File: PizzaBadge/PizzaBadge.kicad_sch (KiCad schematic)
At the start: 169 parts, among them J1 BATTERY, J2 signal 1, J3 signal 1, J4 signal 1, J5 signal 1, J6 signal 1, J7 signal 1, J8 signal 1, J9 signal 1, Q1 NPN, Q2 NPN, Q3 NPN, Q4 NPN, Q5 NPN, Q6 NPN, Q7 NPN, Q8 NPN

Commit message: fix scheme, fix board, add reset button, revision1
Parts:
- added J10: signal 1, Connector_PinHeader_2.54mm:PinHeader_1x01_P2.54mm_Vertical, symbol Connector:Conn_01x01_Female
- added R81: 1K, Resistor_THT:R_Axial_DIN0204_L3.6mm_D1.6mm_P7.62mm_Horizontal, symbol Device:R
- added SW1: RESET, Button_Switch_SMD:SW_SPST_CK_RS282G05A3, symbol Switch:SW_Push
- R10, R20, R30, R39, R50, R60, R70, R80: value 4k7 -> 1K
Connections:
- net GND: now also D19.1 (K), D20.1 (K), D21.1 (K), D22.1 (K), D23.1 (K), D24.1 (K), D25.1 (K), D26.1 (K), D27.1 (K), D28.1 (K), D29.1 (K), D30.1 (K), D31.1 (K), D32.1 (K), D33.1 (K), D34.1 (K), D35.1 (K), D36.1 (K), D37.1 (K), D38.1 (K), D39.1 (K), D40.1 (K), D41.1 (K), D42.1 (K), D43.1 (K), D44.1 (K), D45.1 (K), D46.1 (K), D47.1 (K), D48.1 (K), D49.1 (K), D50.1 (K), D51.1 (K), D52.1 (K), D53.1 (K), D54.1 (K), D55.1 (K), D56.1 (K), D57.1 (K), D58.1 (K), D59.1 (K), D60.1 (K), D61.1 (K), D62.1 (K), D63.1 (K), D64.1 (K), D65.1 (K), D66.1 (K), D67.1 (K), D68.1 (K), D69.1 (K), D70.1 (K), D71.1 (K), D72.1 (K), SW1.1
- net 12V renamed 5V
- net 5V: now also R81.2
- new net RESET: J10.1 (Pin_1), R81.1, SW1.2
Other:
- moved on the sheet: J1

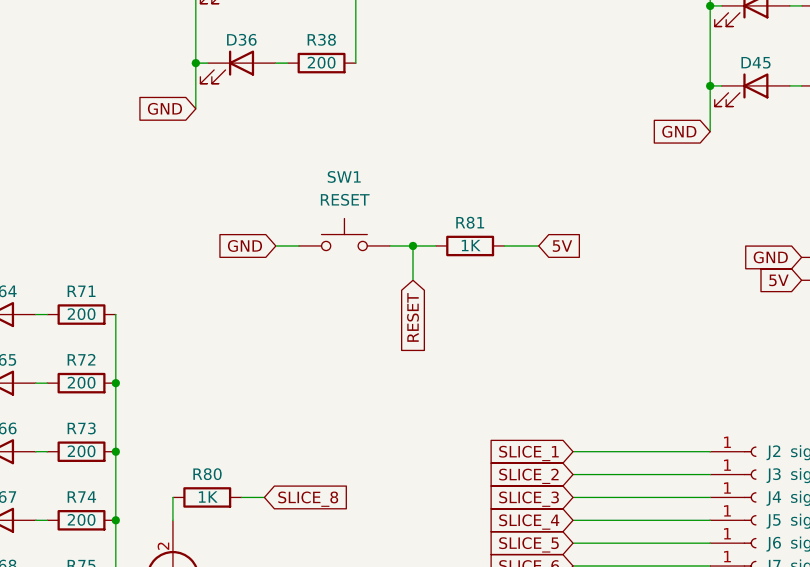
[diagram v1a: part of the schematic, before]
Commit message: add reset button
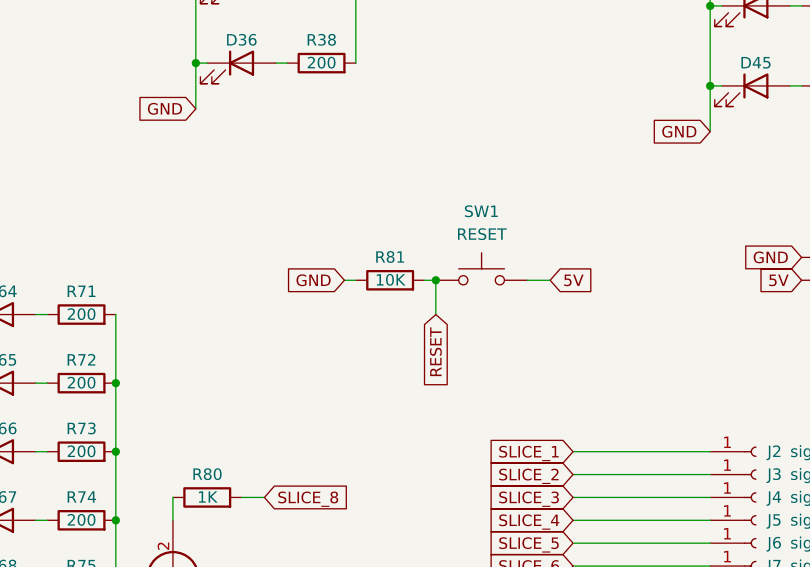
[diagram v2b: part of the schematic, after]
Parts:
- R81: value 1K -> 10K
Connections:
- net 5V: now also SW1.2; no longer R81.2
- net GND: now also R81.1; no longer SW1.1
- net RESET: now also R81.2, SW1.1; no longer R81.1, SW1.2
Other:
- moved on the sheet: R81, SW1
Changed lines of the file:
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@@
   (junction (at 69.85 44.45) (diameter 0) (color 0 0 0 0)
   )
-  (junction (at 194.31 105.41) (diameter 0) (color 0 0 0 0)
-  )
   (junction (at 69.85 67.31) (diameter 0) (color 0 0 0 0)
   )
@@
   (junction (at 87.63 76.2) (diameter 0) (color 0 0 0 0)
   )
+  (junction (at 196.85 109.22) (diameter 0) (color 0 0 0 0)
+  )
   (junction (at 143.51 176.53) (diameter 0) (color 0 0 0 0)
   )
@@
     (stroke (width 0) (type default) (color 0 0 0 0))
   )
+  (wire (pts (xy 196.85 109.22) (xy 196.85 113.03))
+    (stroke (width 0) (type default) (color 0 0 0 0))
+  )
   (wire (pts (xy 161.29 143.51) (xy 162.56 143.51))
     (stroke (width 0) (type default) (color 0 0 0 0))
@@
     (stroke (width 0) (type default) (color 0 0 0 0))
   )
-  (wire (pts (xy 191.77 105.41) (xy 194.31 105.41))
-    (stroke (width 0) (type default) (color 0 0 0 0))
-  )
   (wire (pts (xy 179.07 44.45) (xy 180.34 44.45))
     (stroke (width 0) (type default) (color 0 0 0 0))
@@
     (stroke (width 0) (type default) (color 0 0 0 0))
   )
-  (wire (pts (xy 194.31 105.41) (xy 196.85 105.41))
-    (stroke (width 0) (type default) (color 0 0 0 0))
-  )
   (wire (pts (xy 39.37 67.31) (xy 39.37 76.2))
     (stroke (width 0) (type default) (color 0 0 0 0))
@@
     (stroke (width 0) (type default) (color 0 0 0 0))
   )
-  (wire (pts (xy 179.07 105.41) (xy 181.61 105.41))
-    (stroke (width 0) (type default) (color 0 0 0 0))
-  )
   (wire (pts (xy 30.48 36.83) (xy 31.75 36.83))
     (stroke (width 0) (type default) (color 0 0 0 0))
@@
     (stroke (width 0) (type default) (color 0 0 0 0))
   )
-  (wire (pts (xy 204.47 105.41) (xy 208.28 105.41))
-    (stroke (width 0) (type default) (color 0 0 0 0))
-  )
   (wire (pts (xy 123.19 29.21) (xy 121.92 29.21))
     (stroke (width 0) (type default) (color 0 0 0 0))
@@
     (stroke (width 0) (type default) (color 0 0 0 0))
   )
+  (wire (pts (xy 207.01 109.22) (xy 209.55 109.22))
+    (stroke (width 0) (type default) (color 0 0 0 0))
+  )
   (wire (pts (xy 92.71 119.38) (xy 93.98 119.38))
     (stroke (width 0) (type default) (color 0 0 0 0))
@@
     (stroke (width 0) (type default) (color 0 0 0 0))
   )
+  (wire (pts (xy 195.58 109.22) (xy 196.85 109.22))
+    (stroke (width 0) (type default) (color 0 0 0 0))
+  )
   (wire (pts (xy 245.11 24.13) (xy 245.11 31.75))
     (stroke (width 0) (type default) (color 0 0 0 0))
@@
     (stroke (width 0) (type default) (color 0 0 0 0))
   )
+  (wire (pts (xy 186.69 109.22) (xy 187.96 109.22))
+    (stroke (width 0) (type default) (color 0 0 0 0))
+  )
   (wire (pts (xy 21.59 59.69) (xy 21.59 67.31))
     (stroke (width 0) (type default) (color 0 0 0 0))
@@
     (stroke (width 0) (type default) (color 0 0 0 0))
   )
-  (wire (pts (xy 194.31 105.41) (xy 194.31 109.22))
-    (stroke (width 0) (type default) (color 0 0 0 0))
-  )
   (wire (pts (xy 194.31 41.91) (xy 194.31 44.45))
     (stroke (width 0) (type default) (color 0 0 0 0))
@@
     )
   )
-  (global_label "RESET" (shape input) (at 194.31 109.22 270) (fields_autoplaced)
+  (global_label "RESET" (shape input) (at 196.85 113.03 270) (fields_autoplaced)
     (effects (font (size 1.27 1.27)) (justify right))
-    (property "Intersheet References" "${INTERSHEET_REFS}" (id 0) (at 194.2306 117.3783 90)
+    (property "Intersheet References" "${INTERSHEET_REFS}" (id 0) (at 196.7706 121.1883 90)
       (effects (font (size 1.27 1.27)) (justify right) hide)
     )
@@
     )
   )
-  (global_label "5V" (shape input) (at 208.28 105.41 0) (fields_autoplaced)
+  (global_label "5V" (shape input) (at 209.55 109.22 0) (fields_autoplaced)
     (effects (font (size 1.27 1.27)) (justify left))
-    (property "Intersheet References" "${INTERSHEET_REFS}" (id 0) (at 212.9912 105.3306 0)
+    (property "Intersheet References" "${INTERSHEET_REFS}" (id 0) (at 214.2612 109.1406 0)
       (effects (font (size 1.27 1.27)) (justify left) hide)
     )
@@
     )
   )
-  (global_label "GND" (shape input) (at 179.07 105.41 180) (fields_autoplaced)
+  (global_label "GND" (shape input) (at 186.69 109.22 180) (fields_autoplaced)
     (effects (font (size 1.27 1.27)) (justify right))
-    (property "Intersheet References" "${INTERSHEET_REFS}" (id 0) (at 172.7864 105.3306 0)
+    (property "Intersheet References" "${INTERSHEET_REFS}" (id 0) (at 180.4064 109.1406 0)
       (effects (font (size 1.27 1.27)) (justify right) hide)
     )
@@
     (pin "2")
   )
-  (symbol (lib_id "Device:R") (at 200.66 105.41 90) (unit 1)
+  (symbol (lib_id "Device:R") (at 191.77 109.22 90) (unit 1)
     (in_bom yes) (on_board yes)
-    (property "Reference" "R81" (id 0) (at 200.66 102.87 90))
-    (property "Value" "1K" (id 1) (at 200.66 105.41 90))
-    (property "Footprint" "Resistor_THT:R_Axial_DIN0204_L3.6mm_D1.6mm_P7.62mm_Horizontal" (id 2) (at 200.66 107.188 90)
+    (property "Reference" "R81" (id 0) (at 191.77 106.68 90))
+    (property "Value" "10K" (id 1) (at 191.77 109.22 90))
+    (property "Footprint" "Resistor_THT:R_Axial_DIN0204_L3.6mm_D1.6mm_P7.62mm_Horizontal" (id 2) (at 191.77 110.998 90)
       (effects (font (size 1.27 1.27)) hide)
     )
-    (property "Datasheet" "~" (id 3) (at 200.66 105.41 0)
+    (property "Datasheet" "~" (id 3) (at 191.77 109.22 0)
       (effects (font (size 1.27 1.27)) hide)
     )
@@
     (pin "2")
   )
-  (symbol (lib_id "Switch:SW_Push") (at 186.69 105.41 0) (unit 1)
+  (symbol (lib_id "Switch:SW_Push") (at 201.93 109.22 0) (unit 1)
     (in_bom yes) (on_board yes) (fields_autoplaced)
-    (property "Reference" "SW1" (id 0) (at 186.69 97.79 0))
-    (property "Value" "RESET" (id 1) (at 186.69 100.33 0))
-    (property "Footprint" "Button_Switch_SMD:SW_SPST_CK_RS282G05A3" (id 2) (at 186.69 100.33 0)
+    (property "Reference" "SW1" (id 0) (at 201.93 101.6 0))
+    (property "Value" "RESET" (id 1) (at 201.93 104.14 0))
+    (property "Footprint" "Button_Switch_SMD:SW_SPST_CK_RS282G05A3" (id 2) (at 201.93 104.14 0)
       (effects (font (size 1.27 1.27)) hide)
     )
-    (property "Datasheet" "~" (id 3) (at 186.69 100.33 0)
+    (property "Datasheet" "~" (id 3) (at 201.93 104.14 0)
       (effects (font (size 1.27 1.27)) hide)
     )
@@
     )
     (path "/ab718489-24aa-4a93-afac-c123d685d990"
-      (reference "R81") (unit 1) (value "1K") (footprint "Resistor_THT:R_Axial_DIN0204_L3.6mm_D1.6mm_P7.62mm_Horizontal")
+      (reference "R81") (unit 1) (value "10K") (footprint "Resistor_THT:R_Axial_DIN0204_L3.6mm_D1.6mm_P7.62mm_Horizontal")
     )
     (path "/ed6cd72f-4985-4265-a8c6-e1402f632187"

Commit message: update
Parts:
- J10: value signal 1 -> PIN RESET
- J2: value signal 1 -> 1
- J3: value signal 1 -> 2
- J4: value signal 1 -> 3
- J5: value signal 1 -> 4
- J6: value signal 1 -> 5
- J7: value signal 1 -> 6
- J8: value signal 1 -> 7
- J9: value signal 1 -> 8
- R1, R11, R12, R13, R14, R15, R16, R17, R18, R19, R2, R21, R22, R23, R24, R25, R26, R27, R28, R29, R3, R31, R32, R33, R34, R35, R36, R37, R38, R4, R40, R41, R42, R43, R44, R45, R46, R47, R48, R49, R5, R51, R52, R53, R54, R55, R56, R57, R58, R59, R6, R61, R62, R63, R64, R65, R66, R67, R68, R69, R7, R71, R72, R73, R74, R75, R76, R77, R78, R79, R8, R9: value 200 -> 330
- R10, R20, R30, R39, R50, R60, R70, R80: value 1K -> 10K
